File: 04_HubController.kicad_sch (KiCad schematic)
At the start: 79 parts, among them U16 CYUSB3304-68LTXx, Y1 26MHz

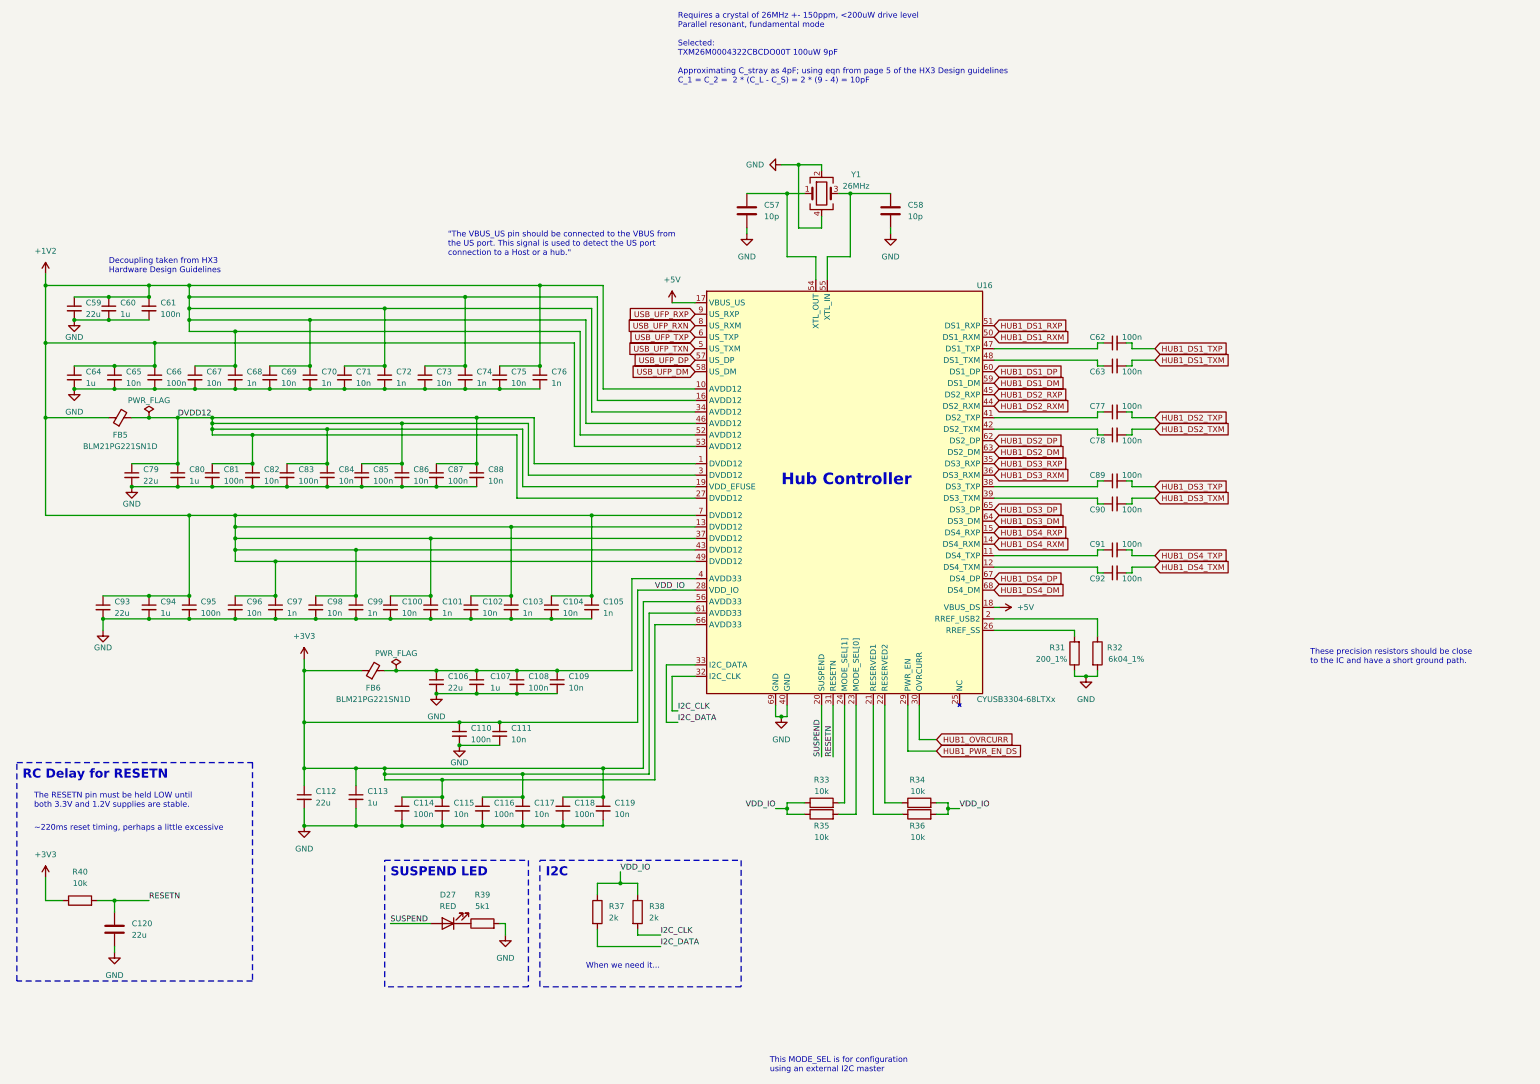
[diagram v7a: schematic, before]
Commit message: add RTL8153
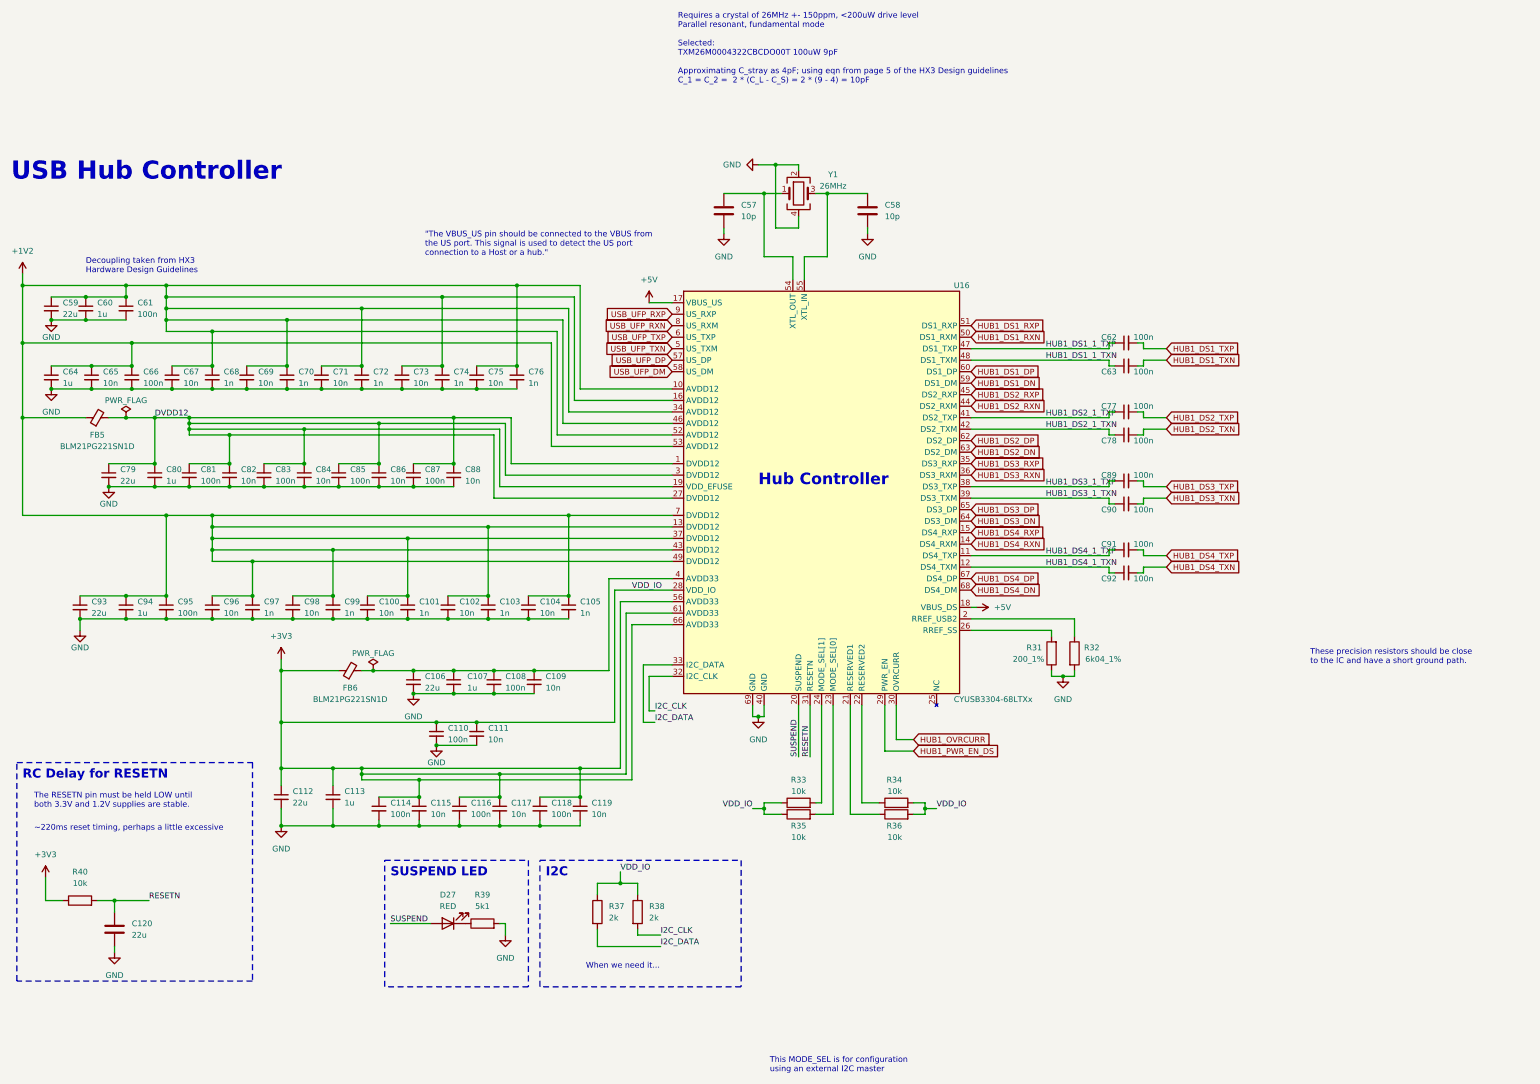
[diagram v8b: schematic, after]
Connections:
- net HUB1_DS3_1_TXP: now reaches C89.1, U16.38 (DS3_TXP)
- net HUB1_DS2_1_TXP: now reaches C77.1, U16.41 (DS2_TXP)
- net HUB1_DS2_1_TXN: now reaches C78.1, U16.42 (DS2_TXM)
- net HUB1_DS4_1_TXP: now reaches C91.1, U16.11 (DS4_TXP)
- net HUB1_DS4_1_TXN: now reaches C92.1, U16.12 (DS4_TXM)
- net HUB1_DS3_1_TXN: now reaches C90.1, U16.39 (DS3_TXM)
- net HUB1_DS1_1_TXP: now reaches C62.1, U16.47 (DS1_TXP)
- net HUB1_DS1_1_TXN: now reaches C63.1, U16.48 (DS1_TXM)
- net HUB1_DS1_DM renamed HUB1_DS1_DN
- net HUB1_DS1_RXM renamed HUB1_DS1_RXN
- net HUB1_DS1_TXM renamed HUB1_DS1_TXN
- net HUB1_DS2_DM renamed HUB1_DS2_DN
- net HUB1_DS2_RXM renamed HUB1_DS2_RXN
- net HUB1_DS2_TXM renamed HUB1_DS2_TXN
- net HUB1_DS3_DM renamed HUB1_DS3_DN
- net HUB1_DS3_RXM renamed HUB1_DS3_RXN
- net HUB1_DS3_TXM renamed HUB1_DS3_TXN
- net HUB1_DS4_DM renamed HUB1_DS4_DN
- net HUB1_DS4_RXM renamed HUB1_DS4_RXN
- net HUB1_DS4_TXM renamed HUB1_DS4_TXN
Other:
- note added: "USB Hub Controller"
- moved on the sheet: C100, C101, C102, C103, C104, C105, C106, C107, C108, C109, C110, C111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
